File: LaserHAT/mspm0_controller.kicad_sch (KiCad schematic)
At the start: 12 parts, among them SW6 BSL, SW7 BL-DT (LCSC C53223909), SW8 BACK, SW9 FIRE, U5 AP2171W, U7 MSPM0G3507SRHBR

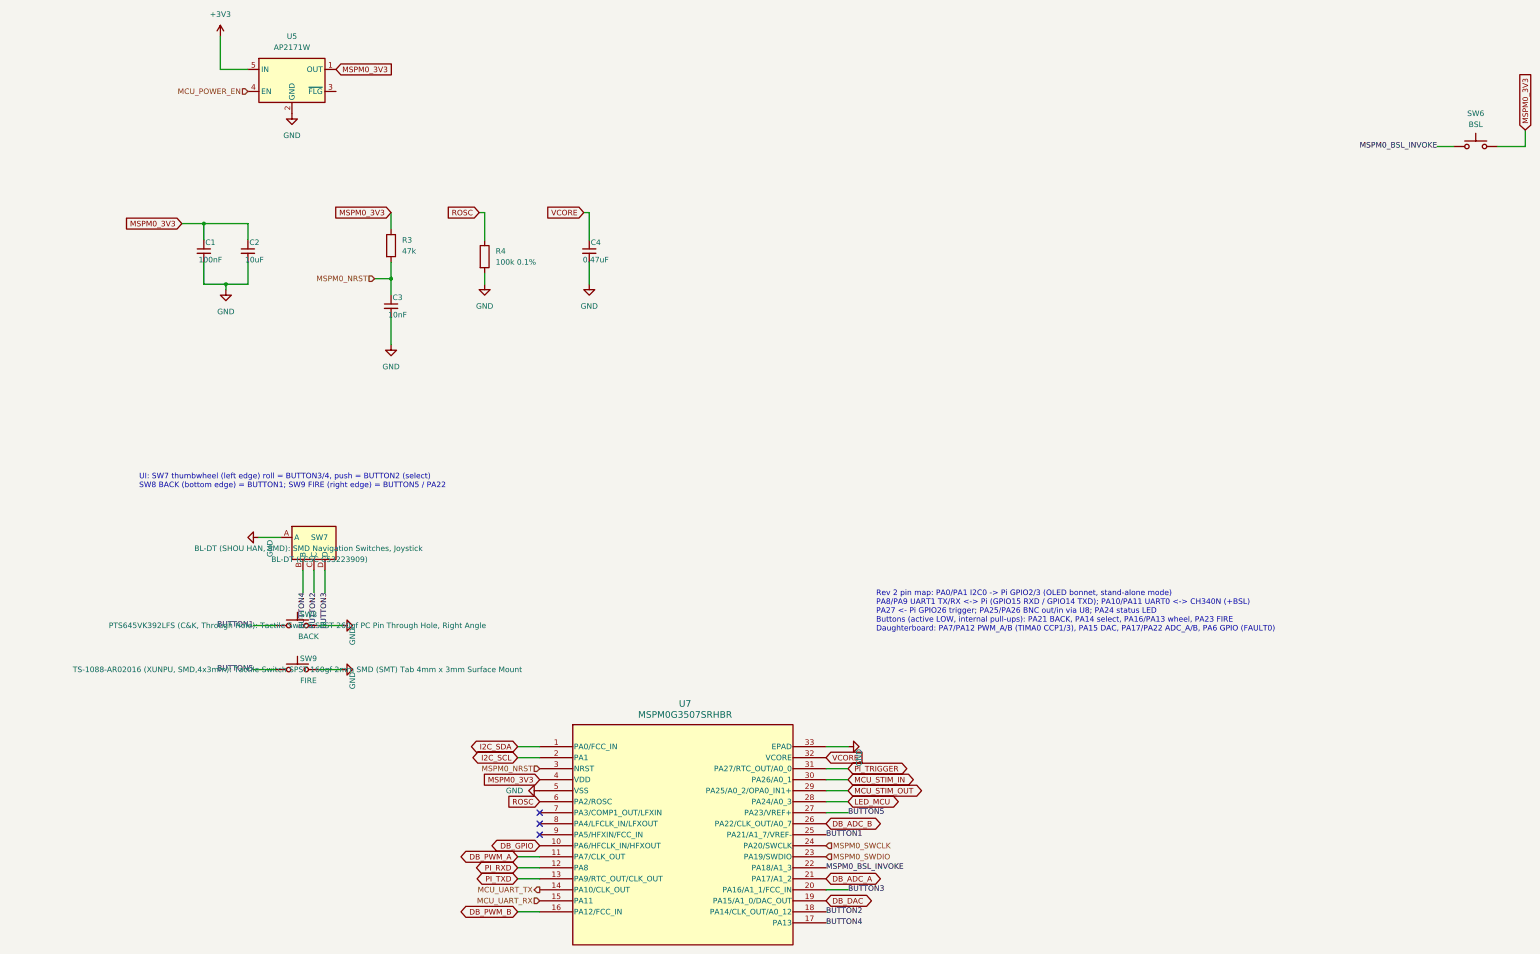
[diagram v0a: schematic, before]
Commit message: LaserHAT: SW8 BACK -> Panasonic EVQP7A01P side-actuated SMD (C79167); Values = part numbers; stamp clears flags
- SW8: schematic footprint Button_Switch_SMD:SW_SPST_EVQP7A; board footprint swapped at the south
  edge (111.55, 98.25), body flush with the edge, button ~0.35 mm proud; BUTTON1 via at the old
  THT pin joins the hand-routed B.Cu run, pad-1 pair bridged; GND pads on the pour. DRC identical
  to before the swap, 0 unconnected; backup stash/LaserDriver_user_2026-09-30_pre-sw8smd.kicad_pcb
- stamp_lcsc.py now also clears DNP / exclude flags on machine-placed parts (SW8 had stayed
  excluded after the previous commit, which wrongly claimed 43 placements)
- Values of LEDs and switches are the part numbers (KT-0603R/W, TS-1088-AR02016, MSK12C02,
  BL-DT, EVQP7A01P, PCM12SMTR) so JLC's BOM matcher sees one part per line; the function names
  remain as silkscreen texts
- verified: lcsc_verify 0 mismatches, sync_check 0 differences (HAT, laser), toolkit BOM/CPL
  consistent in both DNP modes (HAT 29 lines / 43 placements); fab outputs regenerated; docs

Co-Authored-By: Claude Fable 5.1 <noreply@anthropic.com>
Claude-Session: https://claude.ai/code/session_018vgLizGzYPynnY93ajvoVA
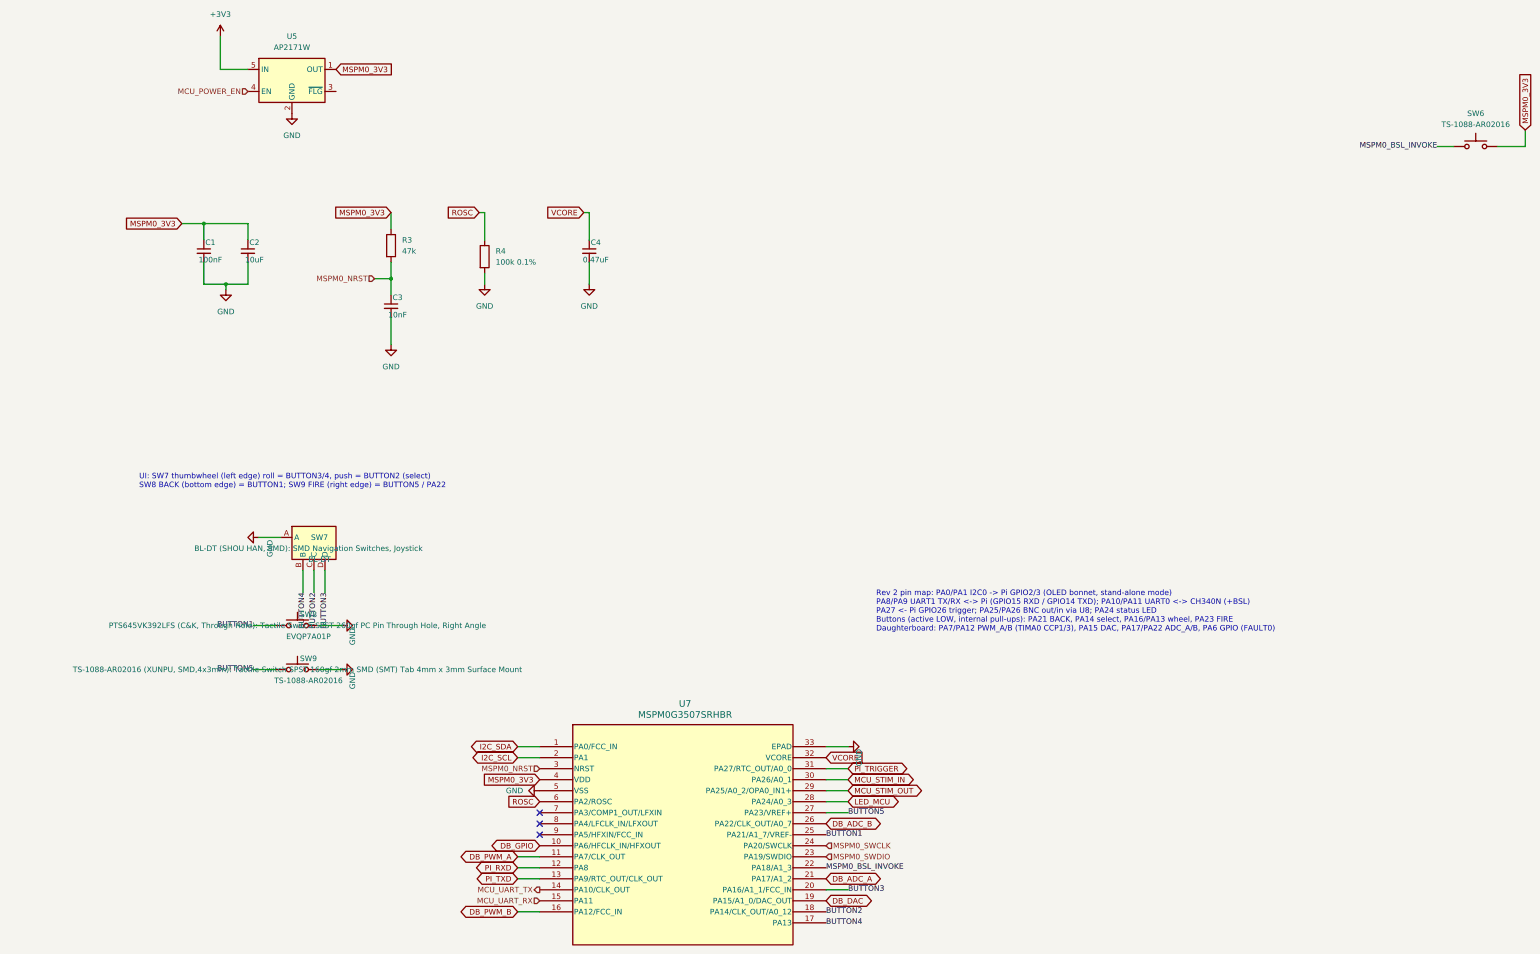
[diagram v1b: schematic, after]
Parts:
- SW6: value BSL -> TS-1088-AR02016
- SW7: value BL-DT (LCSC C53223909) -> BL-DT
- SW8: value BACK -> EVQP7A01P; footprint Button_Switch_THT:SW_Tactile_SPST_Angled_PTS645Vx39-2LFS -> Button_Switch_SMD:SW_SPST_EVQP7A; LCSC Part # C285519 -> C79167; now in the parts list
- SW9: value FIRE -> TS-1088-AR02016
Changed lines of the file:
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@@
 			)
 		)
-		(property "Value" "FIRE"
+		(property "Value" "TS-1088-AR02016"
 			(at 99.06 220.98 0)
 			(effects
@@
 		(unit 1)
 		(exclude_from_sim no)
-		(in_bom no)
+		(in_bom yes)
 		(on_board yes)
 		(dnp no)
@@
 			)
 		)
-		(property "Value" "BACK"
+		(property "Value" "EVQP7A01P"
 			(at 99.06 210.82 0)
 			(effects
@@
 			)
 		)
-		(property "Footprint" "Button_Switch_THT:SW_Tactile_SPST_Angled_PTS645Vx39-2LFS"
+		(property "Footprint" "Button_Switch_SMD:SW_SPST_EVQP7A"
 			(at 96.52 208.28 0)
 			(effects
@@
 			)
 		)
-		(property "LCSC Part #" "C285519"
+		(property "LCSC Part #" "C79167"
 			(at 96.52 208.28 0)
 			(effects
@@
 			)
 		)
-		(property "Value" "BL-DT (LCSC C53223909)"
+		(property "Value" "BL-DT"
 			(at 101.6 193.04 0)
 			(effects
@@
 			)
 		)
-		(property "Value" "BSL"
+		(property "Value" "TS-1088-AR02016"
 			(at 368.3 92.71 0)
 			(effects
